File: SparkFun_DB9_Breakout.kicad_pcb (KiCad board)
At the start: 4 copper layers, 1 part

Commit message: Renames DE9 footprint/symbol
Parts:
- added FID1: Fiducial_0.5mm, SparkFun-Aesthetic:Fiducial_0.5mm_Mask1mm, F.Cu at (128.3, 72.6)
- added FID2: Fiducial_0.5mm, SparkFun-Aesthetic:Fiducial_0.5mm_Mask1mm, F.Cu at (128.3, 75.2)
- added FID3: Fiducial_0.5mm, SparkFun-Aesthetic:Fiducial_0.5mm_Mask1mm, F.Cu at (143.7, 83.2)
- added FID4: Fiducial_0.5mm, SparkFun-Aesthetic:Fiducial_0.5mm_Mask1mm, F.Cu at (161.8, 125.1)
- added J1: A-DS 09 A/KG-T4S, footprints:CONN_A-DS 09 A&slash_KG-T4S_ASM, F.Cu at (132.9, 104.3)
- added ST1: Stand_off, SparkFun-Hardware:Standoff, F.Cu at (123.7, 74.6)
- added ST2: Stand_off, SparkFun-Hardware:Standoff, F.Cu at (123.7, 81.3)
- added ST3: Stand_off, SparkFun-Hardware:Standoff, F.Cu at (140.6, 125.1)
- added ST4: Stand_off, SparkFun-Hardware:Standoff, F.Cu at (139.0, 84.4)

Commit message: Fixes all symbols and footprint names
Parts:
- J1: value A-DS 09 A/KG-T4S -> DE9-Male
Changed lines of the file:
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@@
 			)
 		)
-		(property "Value" "A-DS 09 A/KG-T4S"
+		(property "Value" "DE9-Male"
 			(at 0 15.4 90)
 			(unlocked yes)
@@
 			)
 		)
-		(property "Datasheet" "A-DS 09 A/KG-T4S"
+		(property "Datasheet" ""
 			(at 0 0 90)
 			(layer "F.Fab")

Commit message: Adds some nets, basic outline
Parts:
- removed ST3, ST4: Stand_off, SparkFun-Hardware:Standoff
- added J2: Conn_01x09, SparkFun-Connector:1x09, B.Cu at (136.4, 118.6)
- FID3, FID4: moved to B.Cu
- J1: value DE9-Male -> DB9-Female; footprint footprints:CONN_A-DS 09 A&slash_KG-T4S_ASM -> DB9_Footprint:DB9; moved to B.Cu
- moved FID2 48.3 mm to (123.7, 123.2)
- moved ST2 41.5 mm to (133.1, 121.7)
- moved FID4 38.1 mm to (123.7, 123.2)
- moved J1 23.8 mm to (109.5, 108.7), turned to -90 degrees
- moved FID1 23.3 mm to (136.7, 94.3)
- moved ST1 22.2 mm to (133.1, 94.8)
- moved FID3 13.1 mm to (136.7, 94.3)
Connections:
- J1 pad 1: unconnected-(J1-DCD-Pad1) -> /DCD
- J1 pad 2: unconnected-(J1-RXD-Pad2) -> /TXD
- J1 pad 3: unconnected-(J1-TXD-Pad3) -> /RXD
- J1 pad 4: unconnected-(J1-DTR-Pad4) -> /DTR
- J1 pad 5: unconnected-(J1-GND-Pad5) -> GND
- J1 pad 6: unconnected-(J1-DSR-Pad6) -> /DSR
- J1 pad 7: unconnected-(J1-RTS-Pad7) -> /CTS
- J1 pad 8: unconnected-(J1-CTS-Pad8) -> /RTS
- J1 pad 9: unconnected-(J1-RI-Pad9) -> /RI
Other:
- board outline added: 22.1 x 31.2 mm

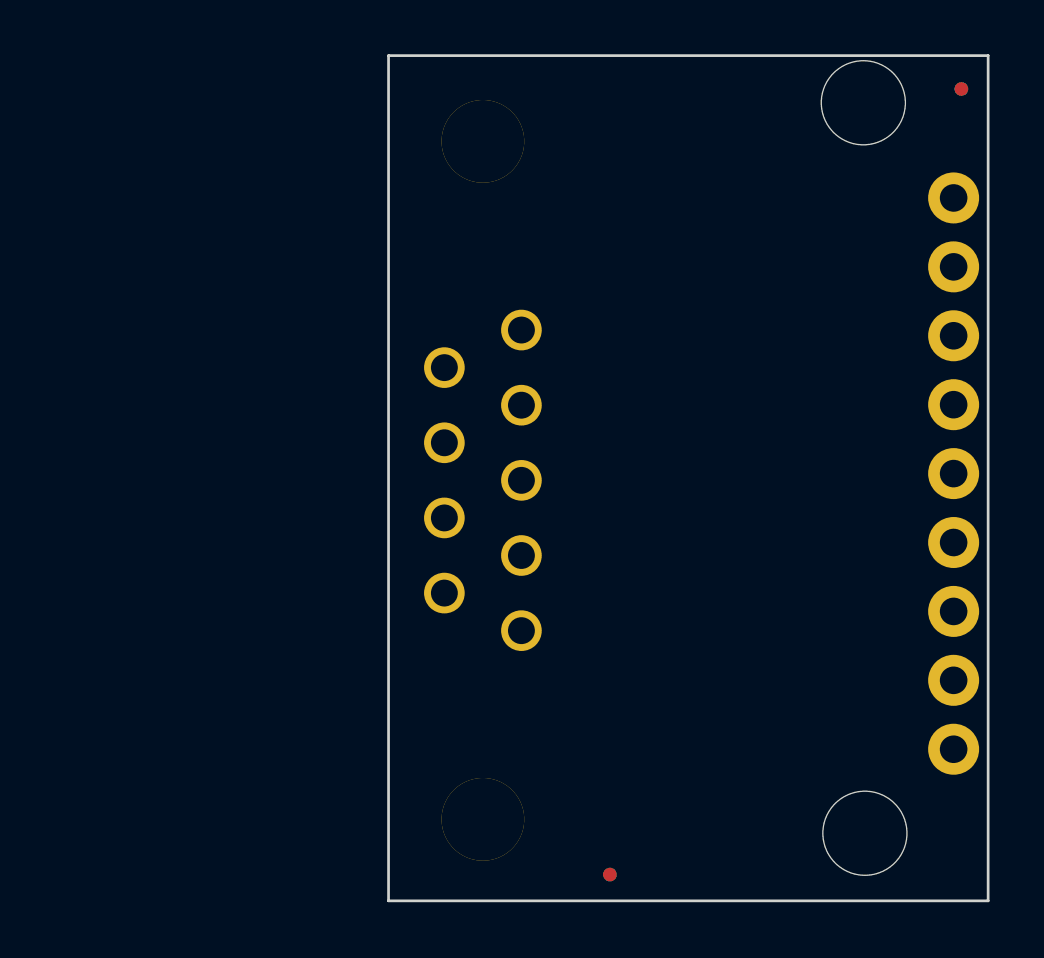
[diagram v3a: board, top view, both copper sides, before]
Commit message: Increases the size of the PCB
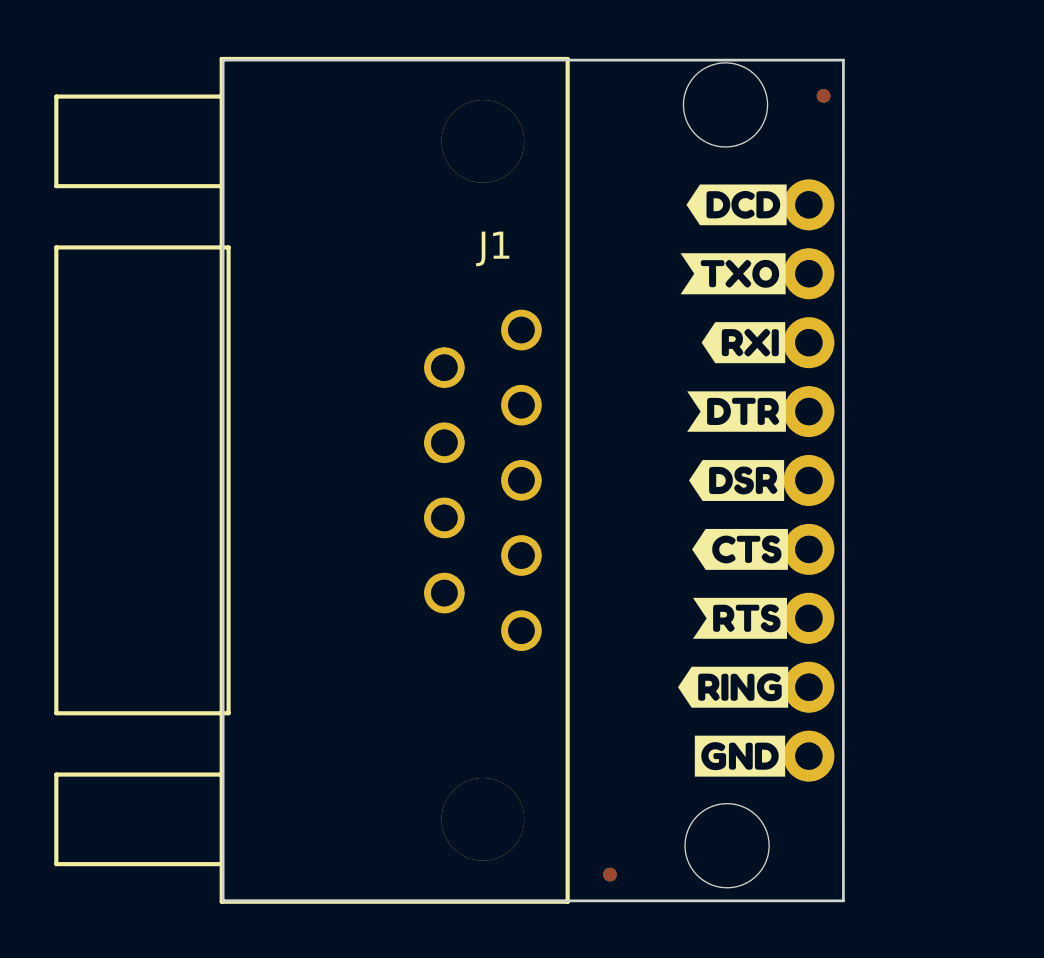
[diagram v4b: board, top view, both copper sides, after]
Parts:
- added kibuzzard-67D1DAAA: G***, kibuzzard-67D1DAAA, F.Cu at (128.5, 118.9)
- added kibuzzard-67D1DAD0: G***, kibuzzard-67D1DAD0, F.Cu at (128.3, 116.3)
- added kibuzzard-67D1DAE5: G***, kibuzzard-67D1DAE5, F.Cu at (128.5, 113.8)
- added kibuzzard-67D1DAFD: G***, kibuzzard-67D1DAFD, F.Cu at (128.5, 111.3)
- added kibuzzard-67D1DB0D: G***, kibuzzard-67D1DB0D, F.Cu at (128.4, 108.7)
- added kibuzzard-67D1DB21: G***, kibuzzard-67D1DB21, F.Cu at (128.4, 106.2)
- added kibuzzard-67D1DB33: G***, kibuzzard-67D1DB33, F.Cu at (128.7, 103.6)
- added kibuzzard-67D1DB48: G***, kibuzzard-67D1DB48, F.Cu at (128.3, 101.1)
- added kibuzzard-67D1DB73: G***, kibuzzard-67D1DB73, F.Cu at (128.4, 98.6)
- J1: moved to F.Cu
- moved J2 20.8 mm to (131.1, 98.6), turned to -90 degrees
- moved ST2 5.10 mm to (128.0, 122.2)
- moved FID1 5.09 mm to (131.6, 94.5)
- moved FID3 5.09 mm to (131.6, 94.5)
- moved ST1 5.08 mm to (128.0, 94.9)
- turned J1 to 90 degrees
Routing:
- added copper zone on B.Cu, net GND
- added copper zone on F.Cu, net GND
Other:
- board size 22.1 x 31.2 mm -> 22.9 x 31 mm
